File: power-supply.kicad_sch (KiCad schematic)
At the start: 19 parts, among them J6 Barrel_Jack_Switch, U3 TD6811, U5 TD6811

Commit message: layouting Power, Motor section
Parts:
- added TP1, TP2, TP3, TP4: TestPoint, TestPoint:TestPoint_Pad_D1.0mm, symbol Connector:TestPoint
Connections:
- net GND: now also TP2.1
- net VIN: now also TP1.1
- net VMCU: now also TP3.1
- net VSOLENOID: now also TP4.1

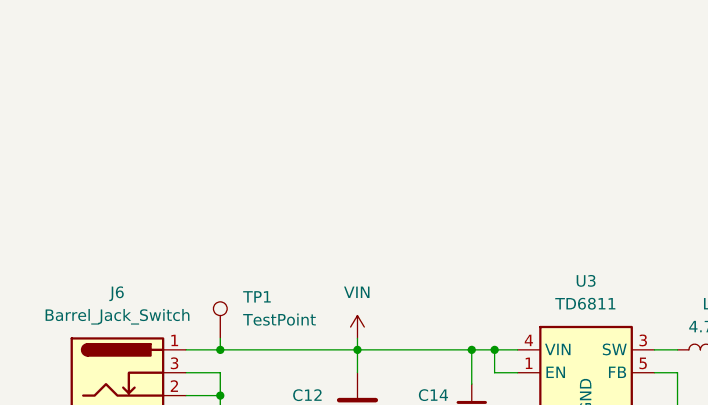
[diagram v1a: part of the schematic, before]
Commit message: Added push button connector
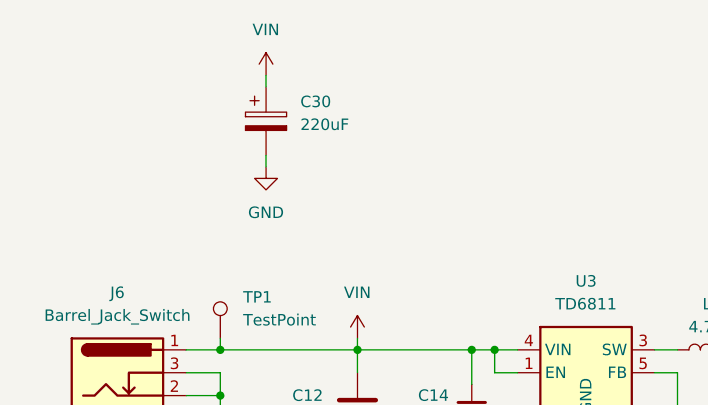
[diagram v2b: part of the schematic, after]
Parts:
- added C30: 220uF, Capacitor_THT:CP_Radial_D6.3mm_P2.50mm, symbol Device:C_Polarized
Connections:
- net GND: now also C30.2
- net VIN: now also C30.1
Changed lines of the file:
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@@
+	(wire
+		(pts
+			(xy 87.63 38.1) (xy 87.63 39.37)
+		)
+		(stroke
+			(width 0)
+			(type default)
+		)
+	)
 	(wire
 		(pts
@@
 		(pts
 			(xy 147.32 119.38) (xy 162.56 119.38)
+		)
+		(stroke
+			(width 0)
+			(type default)
+		)
+	)
+	(wire
+		(pts
+			(xy 87.63 48.26) (xy 87.63 46.99)
 		)
 		(stroke
@@
 	)
 	(symbol
+		(lib_id "Device:C_Polarized")
+		(at 87.63 43.18 0)
+		(unit 1)
+		(exclude_from_sim no)
+		(in_bom yes)
+		(on_board yes)
+		(dnp no)
+		(fields_autoplaced yes)
+		(property "Reference" "C30"
+			(at 91.44 41.0209 0)
+			(effects
+				(font
+					(size 1.27 1.27)
+				)
+				(justify left)
+			)
+		)
+		(property "Value" "220uF"
+			(at 91.44 43.5609 0)
+			(effects
+				(font
+					(size 1.27 1.27)
+				)
+				(justify left)
+			)
+		)
+		(property "Footprint" "Capacitor_THT:CP_Radial_D6.3mm_P2.50mm"
+			(at 88.5952 46.99 0)
+			(effects
+				(font
+					(size 1.27 1.27)
+				)
+				(hide yes)
+			)
+		)
+		(property "Datasheet" "~"
+			(at 87.63 43.18 0)
+			(effects
+				(font
+					(size 1.27 1.27)
+				)
+				(hide yes)
+			)
+		)
+		(property "Description" "Polarized capacitor"
+			(at 87.63 43.18 0)
+			(effects
+				(font
+					(size 1.27 1.27)
+				)
+				(hide yes)
+			)
+		)
+		(pin "1"
+		)
+		(pin "2"
+		)
+		(instances
+			(project "smd-vacuum-controller"
+				(path "/58f4f64d-10fe-43f6-8af4-d87642e52b35/30649fed-d733-46d1-af23-22f75f980e9b"
+					(reference "C30")
+					(unit 1)
+				)
+			)
+		)
+	)
+	(symbol
+		(lib_id "power:+3V3")
+		(at 87.63 38.1 0)
+		(unit 1)
+		(exclude_from_sim no)
+		(in_bom yes)
+		(on_board yes)
+		(dnp no)
+		(fields_autoplaced yes)
+		(property "Reference" "#PWR080"
+			(at 87.63 41.91 0)
+			(effects
+				(font
+					(size 1.27 1.27)
+				)
+				(hide yes)
+			)
+		)
+		(property "Value" "VIN"
+			(at 87.63 33.02 0)
+			(effects
+				(font
+					(size 1.27 1.27)
+				)
+			)
+		)
+		(property "Footprint" ""
+			(at 87.63 38.1 0)
+			(effects
+				(font
+					(size 1.27 1.27)
+				)
+				(hide yes)
+			)
+		)
+		(property "Datasheet" ""
+			(at 87.63 38.1 0)
+			(effects
+				(font
+					(size 1.27 1.27)
+				)
+				(hide yes)
+			)
+		)
+		(property "Description" "Power symbol creates a global label with name \"+3V3\""
+			(at 87.63 38.1 0)
+			(effects
+				(font
+					(size 1.27 1.27)
+				)
+				(hide yes)
+			)
+		)
+		(pin "1"
+		)
+		(instances
+			(project "smd-vacuum-controller"
+				(path "/58f4f64d-10fe-43f6-8af4-d87642e52b35/30649fed-d733-46d1-af23-22f75f980e9b"
+					(reference "#PWR080")
+					(unit 1)
+				)
+			)
+		)
+	)
+	(symbol
 		(lib_id "power:GND")
 		(at 110.49 80.01 0)
@@
 					(unit 1)
 				)
+			)
+		)
+	)
+	(symbol
+		(lib_id "power:GND")
+		(at 87.63 48.26 0)
+		(mirror y)
+		(unit 1)
+		(exclude_from_sim no)
+		(in_bom yes)
+		(on_board yes)
+		(dnp no)
+		(fields_autoplaced yes)
+		(property "Reference" "#PWR082"
+			(at 87.63 54.61 0)
+			(effects
+				(font
+					(size 1.27 1.27)
+				)
+				(hide yes)
+			)
+		)
+		(property "Value" "GND"
+			(at 87.63 53.34 0)
+			(effects
+				(font
+					(size 1.27 1.27)
+				)
+			)
+		)
+		(property "Footprint" ""
+			(at 87.63 48.26 0)
+			(effects
+				(font
+					(size 1.27 1.27)
+				)
+				(hide yes)
+			)
+		)
+		(property "Datasheet" ""
+			(at 87.63 48.26 0)
+			(effects
+				(font
+					(size 1.27 1.27)
+				)
+				(hide yes)
+			)
+		)
+		(property "Description" "Power symbol creates a global label with name \"GND\" , ground"
+			(at 87.63 48.26 0)
+			(effects
+				(font
+					(size 1.27 1.27)
+				)
+				(hide yes)
+			)
+		)
+		(pin "1"
+		)
+		(instances
+			(project "smd-vacuum-controller"
+				(path "/58f4f64d-10fe-43f6-8af4-d87642e52b35/30649fed-d733-46d1-af23-22f75f980e9b"
+					(reference "#PWR082")
+					(unit 1)
+				)
